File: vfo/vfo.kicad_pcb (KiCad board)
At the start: 2 copper layers, 44 x 60 mm, 25 parts, among them J1 CV In, J2 Saw Out, J3 Tri Out, J4 Bus, J5 Conn_01x06, U1 TL072, U2 AS3340

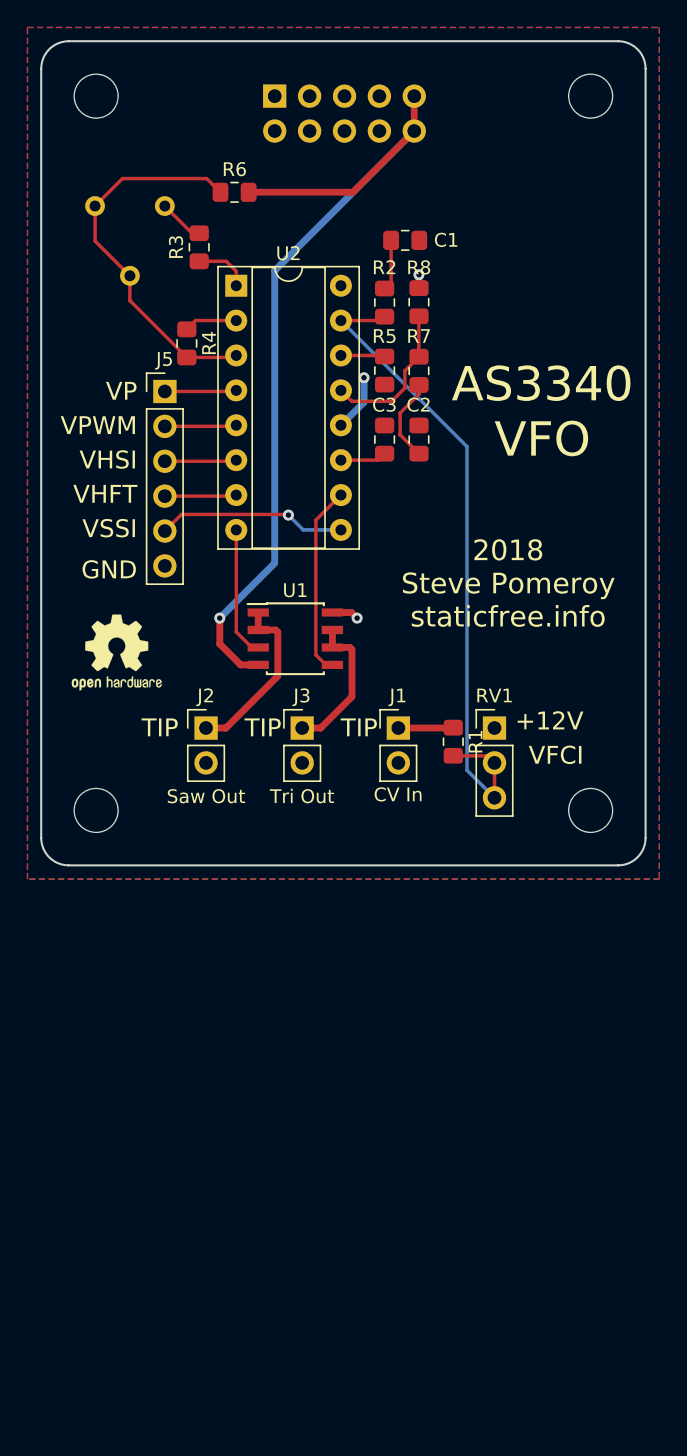
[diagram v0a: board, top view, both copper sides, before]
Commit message: Reworked for 24mm wide
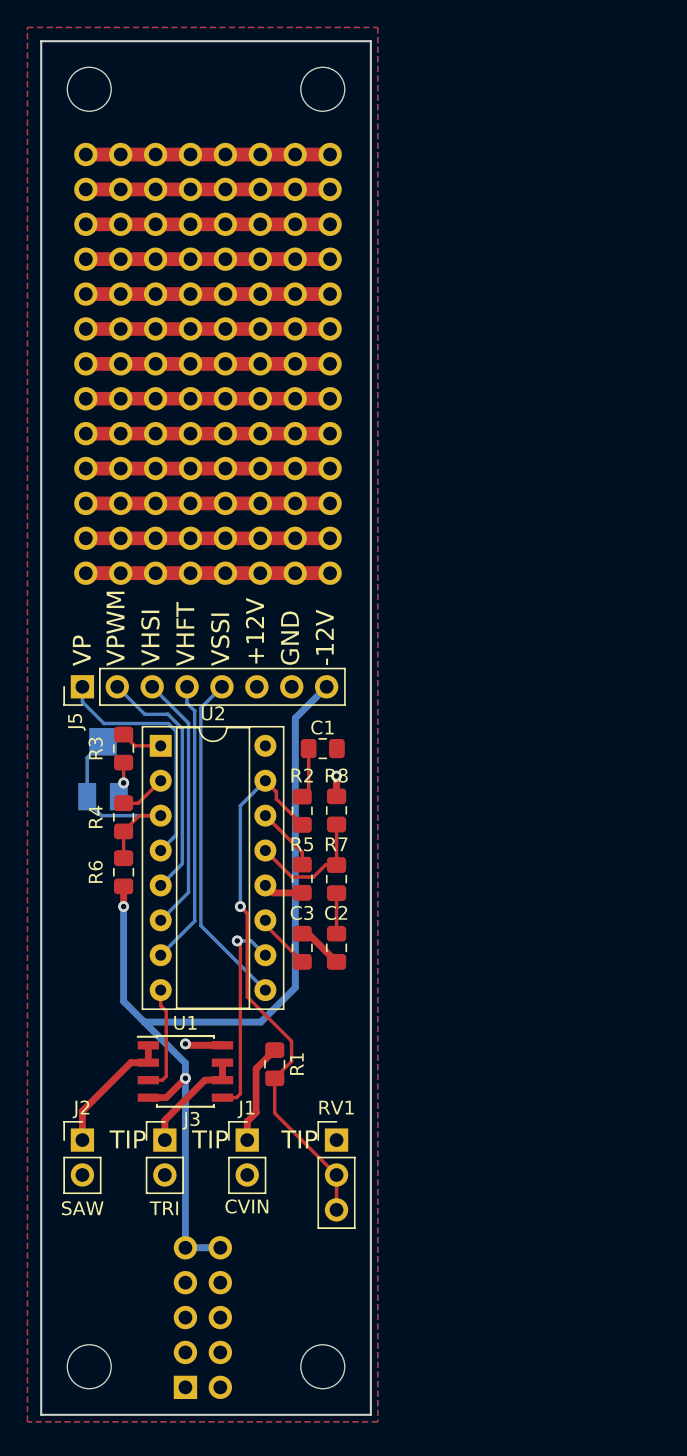
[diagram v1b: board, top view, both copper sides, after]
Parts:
- removed the REF** at (123.0, 76.0)
- removed the REF** at (159.0, 76.0)
- removed the REF** at (159.0, 128.0)
- removed the REF** at (123.0, 128.0)
- removed the REF** at (124.5, 116.5)
- added REF**: MountingHole_3.2mm_M3, MountingHole:MountingHole_3.2mm_M3, F.Cu at (139.5, 168.5)
- added REF**: Breadboard_1x08_P2.54mm, Staticfree:Breadboard_1x08_P2.54mm, F.Cu at (122.2, 90.4)
- added REF**: Breadboard_1x08_P2.54mm, Staticfree:Breadboard_1x08_P2.54mm, F.Cu at (122.2, 87.9)
- added REF**: Breadboard_1x08_P2.54mm, Staticfree:Breadboard_1x08_P2.54mm, F.Cu at (122.2, 85.3)
- added REF**: Breadboard_1x08_P2.54mm, Staticfree:Breadboard_1x08_P2.54mm, F.Cu at (122.2, 82.8)
- added REF**: MountingHole_3.2mm_M3, MountingHole:MountingHole_3.2mm_M3, F.Cu at (122.5, 75.5)
- added REF**: MountingHole_3.2mm_M3, MountingHole:MountingHole_3.2mm_M3, F.Cu at (139.5, 75.5)
- added REF**: MountingHole_3.2mm_M3, MountingHole:MountingHole_3.2mm_M3, F.Cu at (122.5, 168.5)
- added REF**: Breadboard_1x08_P2.54mm, Staticfree:Breadboard_1x08_P2.54mm, F.Cu at (122.2, 80.2)
- added REF**: Breadboard_1x08_P2.54mm, Staticfree:Breadboard_1x08_P2.54mm, F.Cu at (122.2, 110.7)
- added REF**: Breadboard_1x08_P2.54mm, Staticfree:Breadboard_1x08_P2.54mm, F.Cu at (122.2, 108.2)
- added REF**: Breadboard_1x08_P2.54mm, Staticfree:Breadboard_1x08_P2.54mm, F.Cu at (122.2, 105.7)
- added REF**: Breadboard_1x08_P2.54mm, Staticfree:Breadboard_1x08_P2.54mm, F.Cu at (122.2, 103.1)
- added REF**: Breadboard_1x08_P2.54mm, Staticfree:Breadboard_1x08_P2.54mm, F.Cu at (122.2, 100.6)
- added REF**: Breadboard_1x08_P2.54mm, Staticfree:Breadboard_1x08_P2.54mm, F.Cu at (122.2, 98.0)
- added REF**: Breadboard_1x08_P2.54mm, Staticfree:Breadboard_1x08_P2.54mm, F.Cu at (122.2, 95.5)
- added REF**: Breadboard_1x08_P2.54mm, Staticfree:Breadboard_1x08_P2.54mm, F.Cu at (122.2, 93.0)
- J1: value CV In -> CVIN
- J2: value Saw Out -> SAW
- J3: value Tri Out -> TRI
- J4: value Bus -> Conn_02x05_Odd_Even
- J5: value Conn_01x06 -> Conn_01x08; footprint Connector_PinHeader_2.54mm:PinHeader_1x06_P2.54mm_Vertical -> Connector_PinHeader_2.54mm:PinHeader_1x08_P2.54mm_Vertical
- RV2: footprint Potentiometer_THT:Potentiometer_Bourns_3386F_Vertical -> Potentiometer_SMD:Potentiometer_Bourns_3314J_Vertical
- moved J4 94.2 mm to (129.5, 170.0), turned to 0 degrees
- moved R6 50.2 mm to (125.0, 132.5), turned to 270 degrees
- moved RV2 41.2 mm to (123.5, 125.0), turned to 0 degrees
- moved C1 37.5 mm to (139.5, 123.5)
- moved C2 37.5 mm to (140.5, 138.0), turned to 90 degrees
- moved C3 37.5 mm to (138.0, 138.0)
- moved R2 37.5 mm to (138.0, 128.0)
- moved R5 37.5 mm to (138.0, 133.0)
- moved R7 37.5 mm to (140.5, 133.0)
- moved R8 37.5 mm to (140.5, 128.0)
- moved R3 36.9 mm to (125.0, 123.5), turned to 270 degrees
- moved R4 34.8 mm to (125.0, 128.5)
- moved U2 33.9 mm to (127.7, 123.3)
- moved U1 32.5 mm to (129.5, 147.0)
- moved RV1 32.1 mm to (140.5, 152.0)
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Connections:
- J5 pad 6: GND -> +12V
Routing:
- net (no net): track 0.00 -> 231.1 mm
- net /VHFT: track 5.23 -> 20.8 mm
- net /VHSI: track 5.23 -> 18.9 mm
- net /VPWM: track 5.23 -> 18.1 mm
- net /VP: track 5.23 -> 18.0 mm
- net /VEE_R: track 27.8 -> 15.7 mm
- net /VSSI: track 13.8 -> 24.7 mm, vias 1 -> 0
- net /VFCI: track 48.4 -> 40.2 mm, vias 0 -> 1
- net -12V: track 63.1 -> 68.9 mm, vias 1 -> 2
- net /CVIN: track 4.01 -> 7.38 mm
- net Net-(C2-Pad2): track 6.14 -> 2.95 mm
- net /SAW_OUT: track 12.8 -> 9.64 mm
- net /TRI_OUT: track 10.8 -> 8.12 mm
- net GND: track 4.16 -> 6.25 mm, vias 1 -> 0
- net /VLFI: track 11.0 -> 9.29 mm
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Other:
- board size 44 x 60 mm -> 24 x 100 mm
- board text added: "-12V"
- board text removed: "2018 Steve Pomeroy staticfree.info"
- board text removed: "AS3340 VFO"
- board text removed: "VFCI"

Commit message: Update for 19mm width
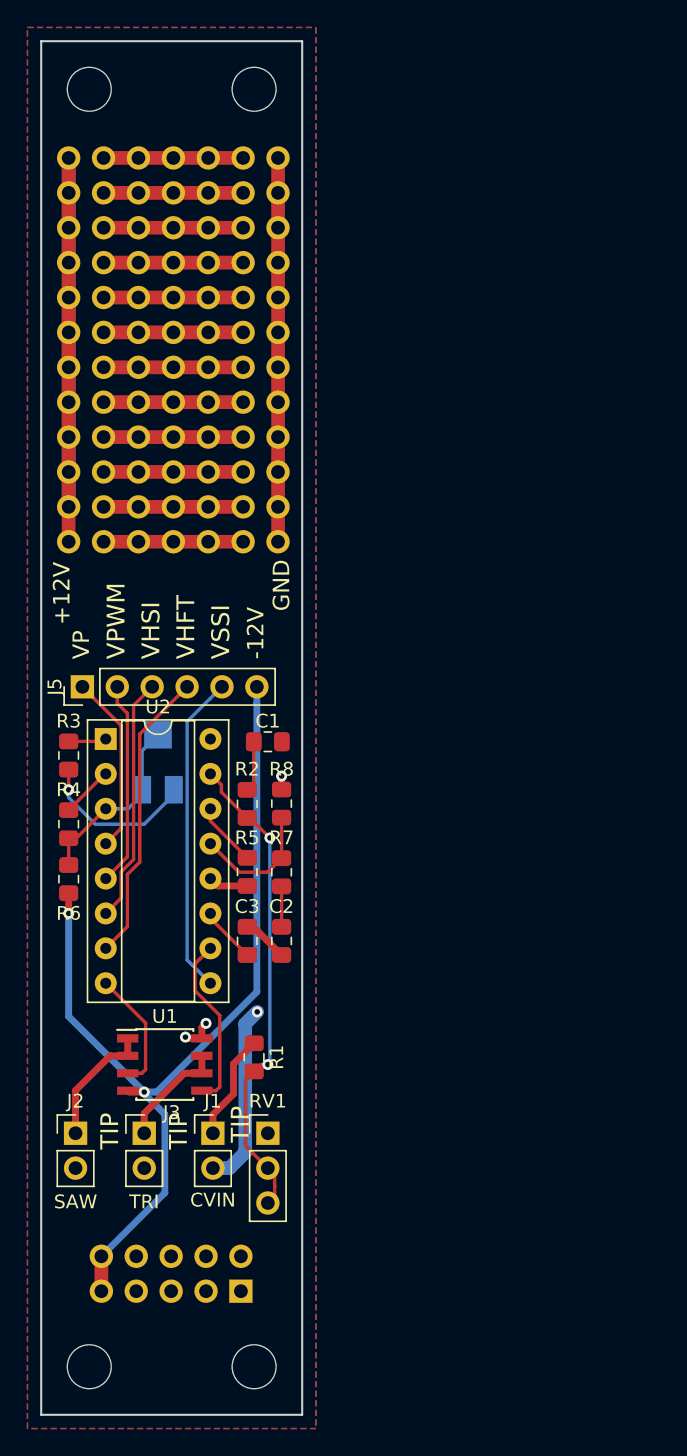
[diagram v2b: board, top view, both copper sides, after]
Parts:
- removed the REF** at (122.2, 90.4)
- removed the REF** at (122.2, 87.9)
- removed the REF** at (122.2, 85.3)
- removed the REF** at (122.2, 82.8)
- removed the REF** at (122.2, 80.2)
- removed the REF** at (122.2, 110.7)
- removed the REF** at (122.2, 108.2)
- removed the REF** at (122.2, 105.7)
- removed the REF** at (122.2, 103.1)
- removed the REF** at (122.2, 100.6)
- removed the REF** at (122.2, 98.0)
- removed the REF** at (122.2, 95.5)
- removed the REF** at (122.2, 93.0)
- added REF**: Breadboard_1x07_P2.54mm, Staticfree:Breadboard_1x07_P2.54mm, F.Cu at (121.0, 108.4)
- added REF**: Breadboard_1x07_P2.54mm, Staticfree:Breadboard_1x07_P2.54mm, F.Cu at (121.0, 85.6)
- added REF**: Breadboard_1x07_P2.54mm, Staticfree:Breadboard_1x07_P2.54mm, F.Cu at (121.0, 83.0)
- added REF**: Breadboard_1x07_P2.54mm, Staticfree:Breadboard_1x07_P2.54mm, F.Cu at (121.0, 80.5)
- added REF**: Breadboard_1x07_P2.54mm, Staticfree:Breadboard_1x07_P2.54mm, F.Cu at (121.0, 105.9)
- added REF**: Breadboard_1x07_P2.54mm, Staticfree:Breadboard_1x07_P2.54mm, F.Cu at (121.0, 103.4)
- added REF**: Breadboard_1x07_P2.54mm, Staticfree:Breadboard_1x07_P2.54mm, F.Cu at (121.0, 100.8)
- added REF**: Breadboard_1x07_P2.54mm, Staticfree:Breadboard_1x07_P2.54mm, F.Cu at (121.0, 98.3)
- added REF**: Breadboard_1x07_P2.54mm, Staticfree:Breadboard_1x07_P2.54mm, F.Cu at (121.0, 95.7)
- added REF**: Breadboard_1x07_P2.54mm, Staticfree:Breadboard_1x07_P2.54mm, F.Cu at (121.0, 93.2)
- added REF**: Breadboard_1x07_P2.54mm, Staticfree:Breadboard_1x07_P2.54mm, F.Cu at (121.0, 90.7)
- added REF**: Breadboard_1x07_P2.54mm, Staticfree:Breadboard_1x07_P2.54mm, F.Cu at (121.0, 88.1)
- J5: value Conn_01x08 -> Conn_01x06; footprint Connector_PinHeader_2.54mm:PinHeader_1x08_P2.54mm_Vertical -> Connector_PinHeader_2.54mm:PinHeader_1x06_P2.54mm_Vertical
- moved J4 8.08 mm to (133.5, 163.0), turned to 90 degrees
- moved RV1 5.02 mm to (135.5, 151.5)
- moved REF** 5.00 mm to (134.5, 75.5)
- moved REF** 5.00 mm to (134.5, 168.5)
- moved C1 4.03 mm to (135.5, 123.0)
- moved C2 4.03 mm to (136.5, 137.5)
- moved C3 4.03 mm to (134.0, 137.5)
- moved R2 4.03 mm to (134.0, 127.5)
- moved R3 4.03 mm to (121.0, 124.0)
- moved R4 4.03 mm to (121.0, 129.0)
- moved R5 4.03 mm to (134.0, 132.5)
- moved R6 4.03 mm to (121.0, 133.0)
- moved R7 4.03 mm to (136.5, 132.5)
- moved R8 4.03 mm to (136.5, 127.5)
- moved RV2 4.03 mm to (127.5, 124.5)
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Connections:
- J5 pad 6: +12V -> -12V
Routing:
- net (no net): track 231.1 -> 121.9 mm
- net +12V: track 4.21 -> 56.8 mm, vias 2 -> 3
- net GND: track 6.25 -> 47.6 mm, vias 0 -> 1
- net /TUNE: track 2.62 -> 11.7 mm
- net /VFCI: track 40.2 -> 34.9 mm, vias 1 -> 2
- net /VP: track 18.0 -> 13.1 mm
- net /VPWM: track 18.1 -> 14.9 mm
- net /VTO: track 15.1 -> 12.7 mm, vias 1 -> 0
- net /VEE_R: track 15.7 -> 13.4 mm
- net /VSSI: track 24.7 -> 23.3 mm
- net /VSO: track 7.86 -> 8.90 mm
- net /VHSI: track 18.9 -> 17.9 mm
- net /VHFT: track 20.8 -> 21.5 mm
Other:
- board size 24 x 100 mm -> 19 x 100 mm
